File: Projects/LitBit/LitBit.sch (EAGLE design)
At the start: 1 part

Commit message: almost milestoneeeE??
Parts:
- removed U$1: ATMEGA32U4-AU, adafruit:ATMEGA32U4-AU
- added C1, C18, C19: 10uF, SCADA_CUSTOM_LIBRARY:CAP_POL_0603
- added C10, C11, C15: 100nF, SCADA_CUSTOM_LIBRARY:CAP_NONPOL_0603
- added C12, C13, C16, C17, C7, C8: 12p, SCADA_CUSTOM_LIBRARY:CAP_NONPOL_0603
- added C14, C26: 1uF, SCADA_CUSTOM_LIBRARY:CAP_NONPOL_0603
- added C2, C25, C3: 4.7uF, SCADA_CUSTOM_LIBRARY:CAP_NONPOL_0603
- added C20: 1 nF, SCADA_CUSTOM_LIBRARY:CAP_NONPOL_0603
- added C21: 1.2 pF, SCADA_CUSTOM_LIBRARY:CAP_NONPOL_0603
- added C22: 1.5 pF, SCADA_CUSTOM_LIBRARY:CAP_NONPOL_0603
- added C23: 1.8 pF, SCADA_CUSTOM_LIBRARY:CAP_NONPOL_0603
- added C24: 2.2 nF, SCADA_CUSTOM_LIBRARY:CAP_NONPOL_0603
- added C27, C4, C5, C6: 100n, SCADA_CUSTOM_LIBRARY:CAP_NONPOL_0603
- added C28, C29: 22p, SCADA_CUSTOM_LIBRARY:CAP_NONPOL_0603
- added C9: 33nF, SCADA_CUSTOM_LIBRARY:CAP_NONPOL_0603
- added D1: Green, Wurth_Elektronik_Optoelectronics_rev18a:WL-SMCW-150060GS75000
- added FB1, FB2: (no value), SCADA_CUSTOM_LIBRARY:FERRITE
- added ISP1: AVRISP-6, adafruit:AVRISP-6
- added JMP1: 0R-JUMPA, SCADA_CUSTOM_LIBRARY:0R-JUMPA
- added JP1, JP10, JP2, JP3, JP4, JP5, JP6, JP7, JP9: (no value), microbuilder:JUMPER2
- added JP11: BLE_SPI, jumper:JP3Q
- added JP12: Display, adafruit:PINHD-1X6
- added JP8: I2c, pinhead:PINHD-1X2
- added L1: 15 nH, SCADA_CUSTOM_LIBRARY:IND-0603
- added L2: 10 uH, SCADA_CUSTOM_LIBRARY:IND-0805
- added L3: 5.6 nH, SCADA_CUSTOM_LIBRARY:IND-0603
- added L4: 8.2 nH, SCADA_CUSTOM_LIBRARY:IND-0603
- added L5: 3.9 nH, SCADA_CUSTOM_LIBRARY:IND-0603
- added R1: 22k, SCADA_CUSTOM_LIBRARY:RES-0603
- added R2, R7: 0R, SCADA_CUSTOM_LIBRARY:RES-0603
- added R3: 47k, SCADA_CUSTOM_LIBRARY:RES-0603
- added R4: 330, SCADA_CUSTOM_LIBRARY:RES-0603
- added R5, R6, R8: 10k, SCADA_CUSTOM_LIBRARY:RES-0603
- added TP1: TEST_POINT_40MIL_DIA, SCADA_CUSTOM_LIBRARY:TEST_POINT_40MIL_DIA
- added U$28: (no value), microbuilder:ANTENNA_PCBNRF8001_1.6MM
- added U1: 24FC1025, SCADA_CUSTOM_LIBRARY:24FC1025
- added U2: MCP7490N, SCADA_CUSTOM_LIBRARY:MCP7490N
- added U3: ADXL345, SCADA_CUSTOM_LIBRARY:ADXL345
- added U4: ATMEGA32U4-AU, SCADA_CUSTOM_LIBRARY:ATMEGA32U4-AU
- added U5: S-1335J33-M5T1U3, SCADA_CUSTOM_LIBRARY:S-1335J33-M5T1U3
- added U6: nRF8001, microbuilder:NRF8001
- added U7: MCP73831, SCADA_CUSTOM_LIBRARY:MCP73831
- added USB1: ZX62-B-5PA, Seeed-Connector:MICRO-USB-SMD(ZX62-B-5PA)
- added Y1: 16.0000 MHz, SCADA_CUSTOM_LIBRARY:FA-238_CRYSTAL
- added Y2, Y3: 32.7680 kHz, SCADA_CUSTOM_LIBRARY:ABS25_CRYSTAL
- added Y4: 8.0000 MHz, adafruit:CRYSTALHC49UP
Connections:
- new net 3.3V: C19.+, FB1.P$1, ISP1.VCC, JMP1-0R.3, JP2.2, JP3.2, JP5.2, JP9.2, R5.2, R6.2, R7.1, U5.VOUT
- new net ACTIVE: U6A.ACTIVE
- new net AGND: R2.1, U3.GND
- new net AVCC: JP10.2, JP7.2, R7.2
- new net D+: U4.D+, USB1.D+
- new net D-: U4.D-, USB1.D-
- new net MFP: R8.1, U2.MFP
- new net MISO: ISP1.MISO, JP11.5
- new net MISO_3V3: JP11.6, U6A.MISO
- new net MOSI: ISP1.MOSI, JP11.3, U4.PB2(PDI/MOSI)
- new net MOSI_3V3: JP11.4, U6A.MOSI
- new net N$1: C7.2, U2.X1, Y3.2
- new net N$10: L1.1, L2.2
- new net N$11: L2.1, U6A.DCC
- new net N$12: C16.1, U6A.XC1, Y1.2
- new net N$13: JMP1-0R.2, U5.SST
- new net N$14: C18.+, JP1.1, U5.ON/OFF, U5.VIN
- new net N$15: C4.1, JP2.1, R8.2, U2.VCC
- new net N$16: C3.1, JP4.1, U7.VBAT
- new net N$17: C26.1, C5.1, JP3.1, U1.A2, U1.VCC
- new net N$18: C17.1, U6A.XC2, Y1.1
- new net N$19: C23.2, L5.2
- new net N$2: C8.2, U2.X2, Y3.1
- new net N$20: L4.2, L5.1, U6A.ANT2
- new net N$21: L3.1, L4.1, U6A.ANT1
- new net N$22: R1.1, U6A.IREF
- new net N$23: C24.1, L3.2, U6A.VDD_PA
- new net N$24: C21.1, C22.1, C23.1, U$28.P$1
- new net N$25: D1.-, R4.2
- new net N$26: R3.2, U7.PROG
- new net N$27: R4.1, U7.STAT
- new net N$28: C25.1, JP9.1, U4.VCC, U4.VCC1
- new net N$29: C28.2, U4.XTAL2, Y4.1
- new net N$3: C10.1, U6A.DEC1
- new net N$30: C29.2, U4.XTAL1, Y4.2
- new net N$32: FB2.P$2, JP10.1
- new net N$33: C27.1, FB2.P$1, U4.AVCC, U4.AVCC1
- new net N$34: TP1.P$1, U4.AREF
- new net N$4: C9.1, U6A.DEC2
- new net N$5: C12.2, U6A.XL2, Y2.2
- new net N$6: C13.2, U6A.XL1, Y2.1
- new net N$7: C2.1, D1.+, JP6.1, U7.VDD
- new net N$8: C1.+, C15.1, JP5.1, U6A.VDD@1, U6A.VDD@2
- new net N$9: C6.2, JP7.1, U3.VS
- new net RDYN: U6A.RDYN
- new net REQN_3V3: U6A.REQN
- new net RST: ISP1.RST, U4./RESET
- new net RST_NRF: U6A.RESET
- new net SCK: ISP1.SCK, JP11.1, U4.PB1(SCK)
- new net SCK_3V3: JP11.2, U6A.SCK
- new net SCL: JP8.2, R5.1, U1.SCL, U2.SCL, U3.SCL, U4.PD0(INT0/OC0B/SCL)
- new net SDA: JP8.1, R6.1, U1.SDA, U2.SDA, U3.SDA, U4.PD1(INT1/SDA)
- new net SHIELD: USB1.GND, USB1.SHIELD
- new net VDDA: C11.1, C14.1, C20.1, FB1.P$2, L1.2, U6A.AVDD@1, U6A.AVDD@2, U6A.AVDD@3
- new net V_BATT: JP1.2, JP4.2
- new net V_USB: JP6.2, U4.VBUS, USB1.VBUS
- net GND: now also C1.-, C10.2, C11.2, C12.1, C13.1, C14.2, C15.2, C16.2, C17.2, C18.-, C19.-, C2.2, C20.2, C21.2, C22.2, C24.2, C25.2, C26.2, C27.2, C28.1, C29.1, C3.2, C4.2, C5.2, C6.1, C7.1, C8.1, C9.2, ISP1.GND, JMP1-0R.1, R1.2, R2.2, R3.1, U1.A0, U1.A1, U1.VSS, U1.WP, U2.VBAT, U2.VSS, U4.GND, U4.GND1, U4.GND2, U4.GND3, U4.UGND, U5.VSS, U6-SLUG.TP, U6A.VSS@1, U6A.VSS@2, U6A.VSS@3, U6A.VSS@4, U6A.VSS@5, U6A.VSS@6, U7.VSS; no longer U$1.GND, U$1.GND1, U$1.GND2, U$1.GND3
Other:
- note added: "SPI MODE 0"
- note added: "but RDYN and REQN"
- note added: "replace CS"

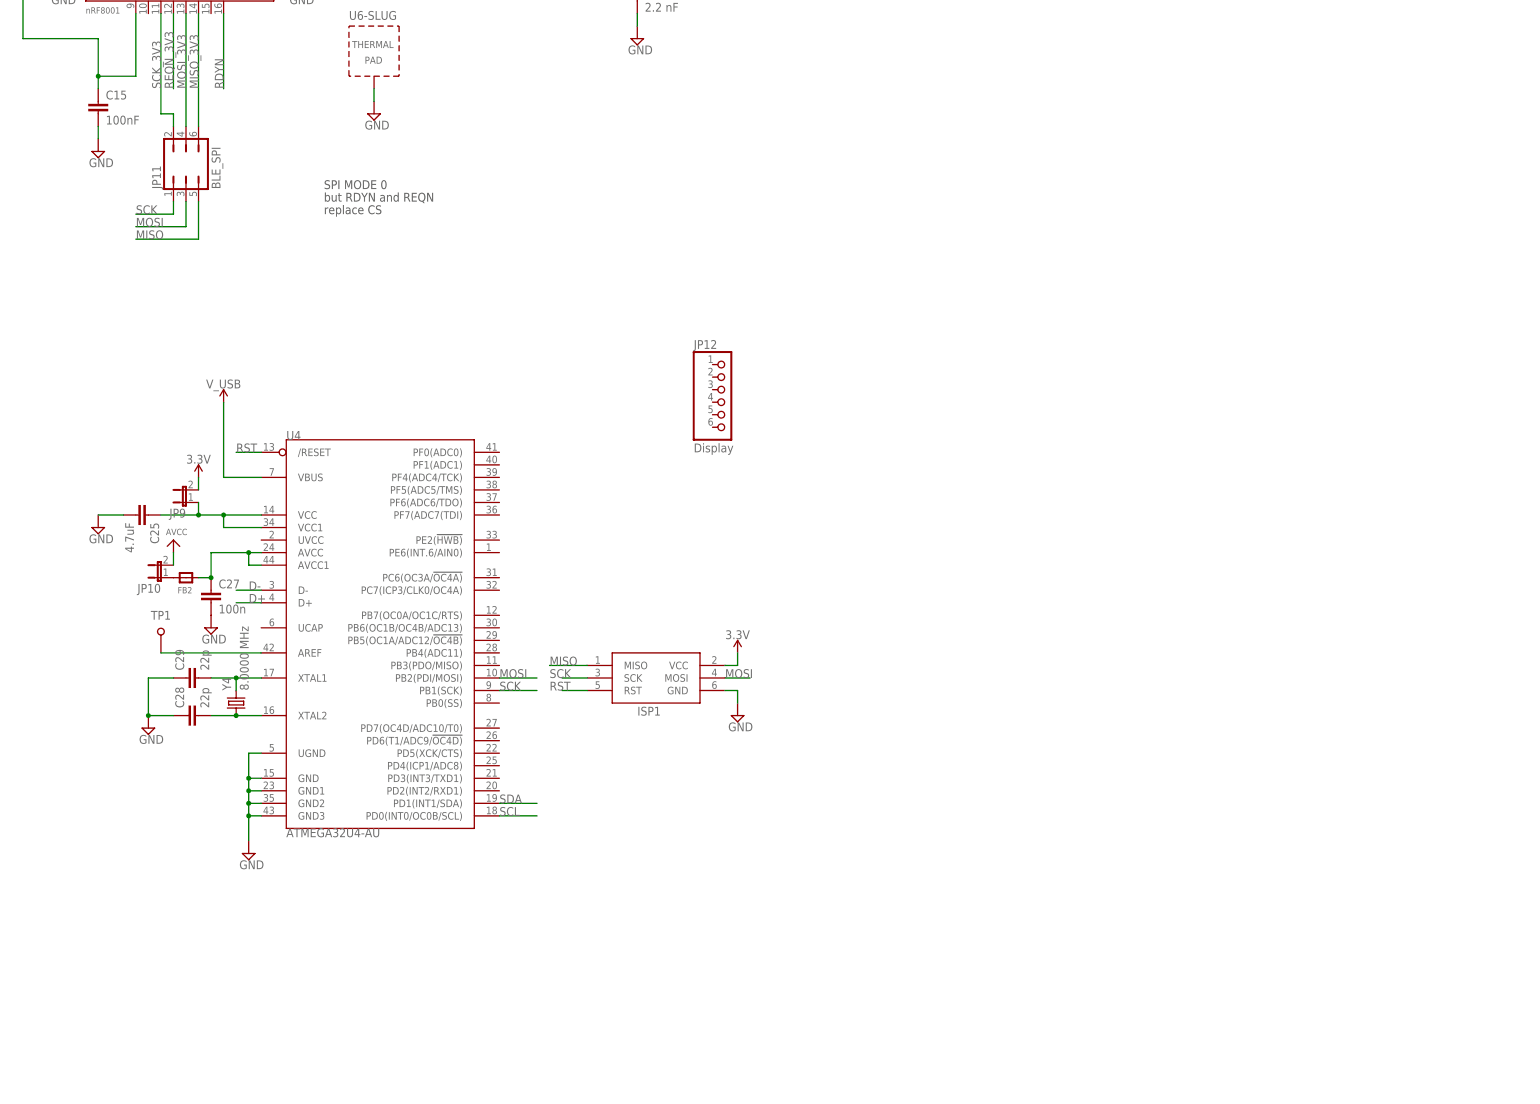
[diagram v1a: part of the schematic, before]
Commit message: Change processor package to VQFN to save space.
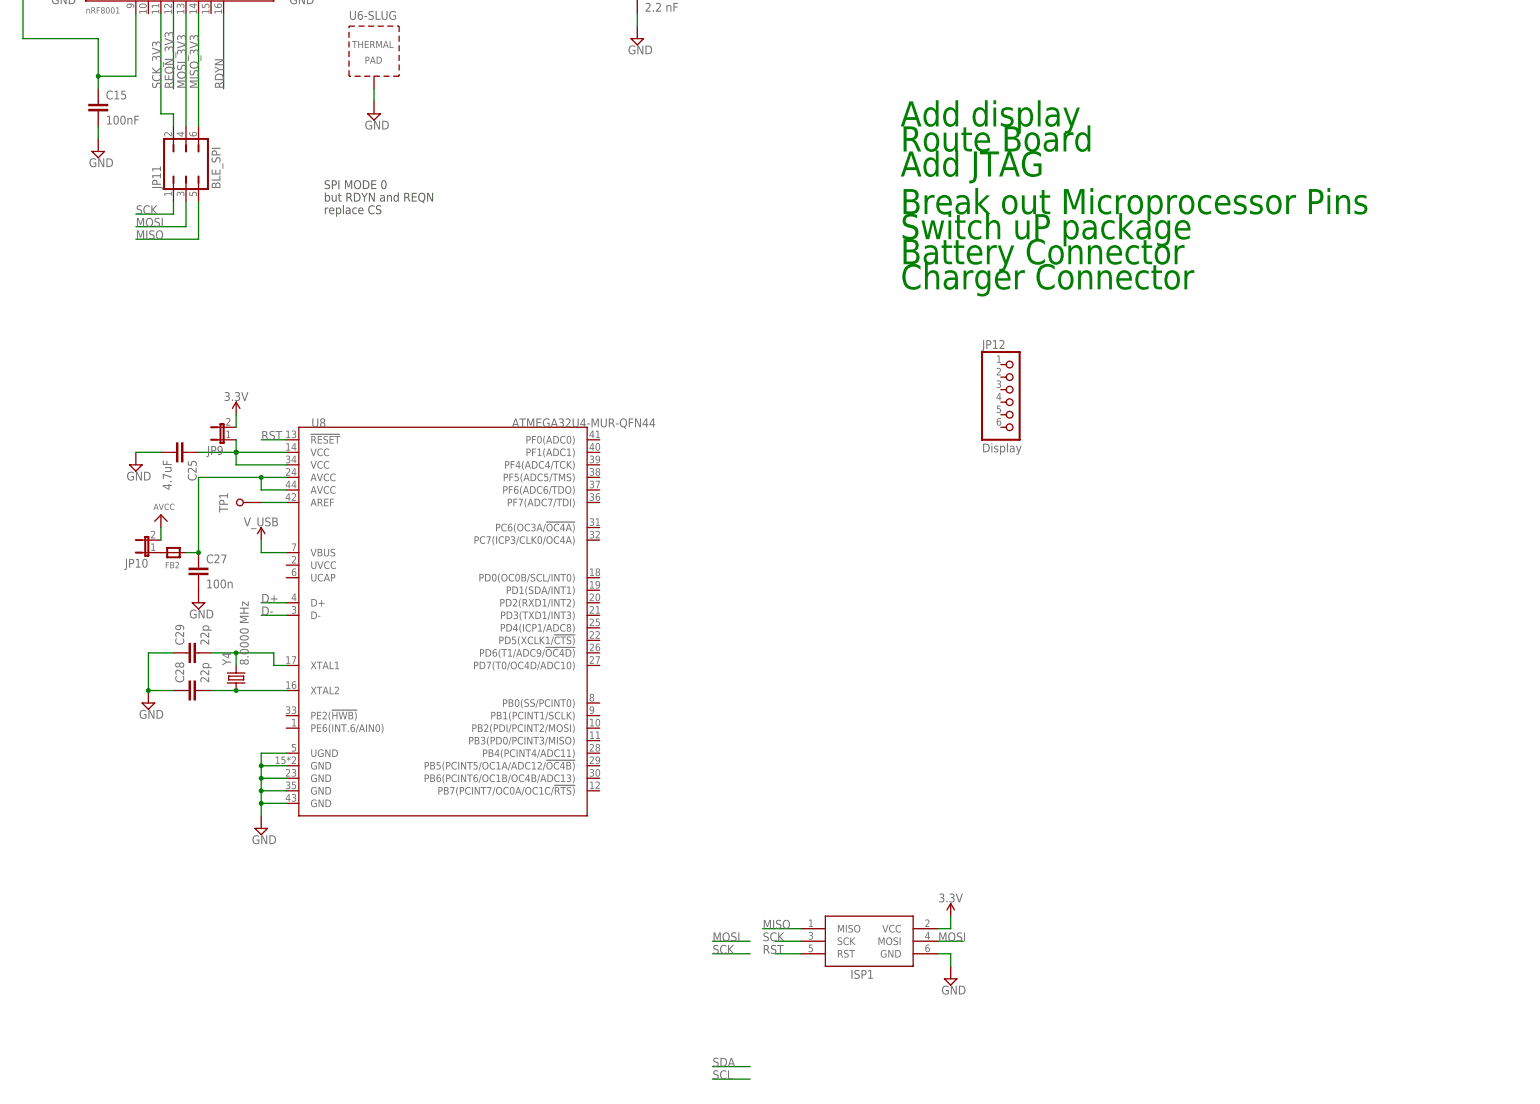
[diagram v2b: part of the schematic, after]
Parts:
- removed U4: ATMEGA32U4-AU, SCADA_CUSTOM_LIBRARY:ATMEGA32U4-AU
- added U8: ATMEGA32U4-MUR-QFN44, Seeed-IC:MCU-ATMEGA32U4-MUR(VQFN44)
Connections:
- net D+: now also U8.D+; no longer U4.D+
- net D-: now also U8.D-; no longer U4.D-
- net GND: now also U8.GND@1, U8.GND@2, U8.GND@3, U8.GND@4, U8.UGND; no longer U4.GND, U4.GND1, U4.GND2, U4.GND3, U4.UGND
- net MOSI: no longer U4.PB2(PDI/MOSI)
- net N$28: now also U8.VCC@1, U8.VCC@2; no longer U4.VCC, U4.VCC1
- net N$29: now also U8.XTAL2; no longer U4.XTAL2
- net N$30: now also U8.XTAL1; no longer U4.XTAL1
- net N$33: now also U8.AVCC@1, U8.AVCC@2; no longer U4.AVCC, U4.AVCC1
- net N$34: no longer U4.AREF
- net RST: now also U8.!RESET; no longer U4./RESET
- net SCK: no longer U4.PB1(SCK)
- net SCL: no longer U4.PD0(INT0/OC0B/SCL)
- net SDA: no longer U4.PD1(INT1/SDA)
- net V_USB: now also U8.VBUS; no longer U4.VBUS
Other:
- note added: "Add JTAG"
- note added: "Add display"
- note added: "Battery Connector"
- note added: "Break out Microprocessor Pins"
- note added: "Charger Connector"
- note added: "Route Board"
- note added: "Switch uP package"
- moved on the sheet: C25, C27, C28, C29, FB2, ISP1, JP10, JP12, JP9, TP1, Y4

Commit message: Start Layout, change uP package, add display, add JTAG, add battery connector.
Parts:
- removed D1: Green, Wurth_Elektronik_Optoelectronics_rev18a:WL-SMCW-150060GS75000
- removed JP10, JP4, JP5, JP6, JP7, JP9: (no value), microbuilder:JUMPER2
- removed JP11: BLE_SPI, jumper:JP3Q
- removed JP12: Display, adafruit:PINHD-1X6
- removed R7: 0R, SCADA_CUSTOM_LIBRARY:RES-0603
- removed TP1: TEST_POINT_40MIL_DIA, SCADA_CUSTOM_LIBRARY:TEST_POINT_40MIL_DIA
- removed Y4: 8.0000 MHz, adafruit:CRYSTALHC49UP
- added C30, C31, C34: 1uF, SCADA_CUSTOM_LIBRARY:CAP_NONPOL_0603
- added C32: 10uF, SCADA_CUSTOM_LIBRARY:CAP_POL_0603
- added C33: 100n, SCADA_CUSTOM_LIBRARY:CAP_NONPOL_0603
- added CHRG: Green, SCADA_CUSTOM_LIBRARY:LED_WL-SMCW-150060GS75000
- added J1: Battery, SparkFun-Connectors:CONN_02-JST-2MM-SMT
- added Q1: CSTCR6M00G53Z, murata-filter:CSTCR6M00G53Z
- added R10, R11, R12, R13, R14, R9: 10k, SCADA_CUSTOM_LIBRARY:RES-0603
- added R15, R16, R17, R18, R19, R20, R21, R22, R23, R24: 0, SCADA_CUSTOM_LIBRARY:RES-0603
- C26: value 1uF -> 4.7 uF
- C28: value 22p -> 100n
- C29: value 22p -> 4.7uF
- JP1: value (none) -> Display; device microbuilder:JUMPER2 -> pinhead:PINHD-1X4
- JP2: device microbuilder:JUMPER2 -> pinhead:PINHD-2X3
- JP3: value (none) -> JTAG; device microbuilder:JUMPER2 -> pinhead:PINHD-2X5
- R5, R6: value 10k -> 2.2k
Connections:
- removed net N$28: C25.1, JP9.1, U8.VCC@1, U8.VCC@2
- removed net N$32: FB2.P$2, JP10.1
- removed net N$33: C27.1, FB2.P$1, U8.AVCC@1, U8.AVCC@2
- removed net N$34: TP1.P$1
- removed net N$9: C6.2, JP7.1, U3.VS
- removed net SHIELD: USB1.GND, USB1.SHIELD
- new net ADXL_INT1: U3.INT1, U8.PD3(TXD1/INT3)
- new net ADXL_INT2: U3.INT2, U8.PD4(ICP1/ADC8)
- new net CHRG_IN: C2.1, CHRG.+, R15.2, U7.VDD
- new net N$36: C32.+, C33.1, C6.2, R21.2, U3.VDD_I/O, U3.VS
- new net TCK: JP3.1, R10.1, U8.PF4(ADC4/TCK)
- new net TDI: JP3.9, R11.1, U8.PF7(ADC7/TDI)
- new net TDO: JP3.3, R12.1, U8.PF6(ADC6/TDO)
- new net TMS: JP3.5, R9.1, U8.PF5(ADC5/TMS)
- new net UP_AVCC: C27.1, C29.2, R23.2, U8.AVCC@1, U8.AVCC@2
- new net UP_D+: R14.1, U8.D+
- new net UP_D-: R13.1, U8.D-
- new net UP_PWR: C25.1, C28.1, C30.2, JP3.4, R10.2, R11.2, R12.2, R22.2, R9.2, U8.UCAP, U8.VCC@1, U8.VCC@2
- new net UVCC: U8.UVCC
- net 3.3V: now also FB2.P$2, R18.1, R19.1, R20.1, R22.1, R24.1, U3./CS; no longer JP2.2, JP3.2, JP5.2, JP9.2, R7.1
- net ACTIVE: now also U8.PB7(PCINT7/OC0A/OC1C/!RTS)
- net AGND: now also C27.2, C29.1, C32.-, C33.2, C34.2, C6.1, R2.2, U8.AREF; no longer R2.1
- net AVCC: now also C34.1, FB2.P$1, R21.1, R23.1; no longer JP10.2, JP7.2, R7.2
- net D+: now also R14.2; no longer U8.D+
- net D-: now also R13.2; no longer U8.D-
- net GND: now also C28.2, C30.1, C31.2, J1.1, JP1.4, JP3.10, JP3.2, Q1.2, R2.1, U3.SDO, USB1.GND, USB1.SHIELD; no longer C27.2, C28.1, C29.1, C6.1, R2.2
- net MISO: now also JP2.2, U8.PB3(PD0/PCINT3/MISO); no longer JP11.5
- net MISO_3V3: now also JP2.1; no longer JP11.6
- net MOSI: now also JP2.4, U8.PB2(PDI/PCINT2/MOSI); no longer JP11.3
- net MOSI_3V3: now also JP2.3; no longer JP11.4
- net N$14: now also R17.2; no longer JP1.1
- net N$15: now also R19.2; no longer JP2.1
- net N$16: now also R16.2; no longer JP4.1
- net N$17: now also R20.2; no longer JP3.1
- net N$25: now also CHRG.-; no longer D1.-
- net N$29: now also Q1.1, U8.XTAL1; no longer C28.2, U8.XTAL2, Y4.1
- net N$30: now also Q1.3, U8.XTAL2; no longer C29.2, U8.XTAL1, Y4.2
- net N$7: now also JP1.3, R24.2; no longer C2.1, D1.+, JP6.1, U7.VDD
- net N$8: now also R18.2; no longer JP5.1
- net RDYN: now also U8.PD2(RXD1/INT2)
- net RST: now also JP3.6
- net RST_NRF: now also U8.PB0(SS/PCINT0)
- net SCK: now also JP2.6, U8.PB1(PCINT1/SCLK); no longer JP11.1
- net SCK_3V3: now also JP2.5; no longer JP11.2
- net SCL: now also JP1.1, U8.PD0(OC0B/SCL/INT0)
- net SDA: now also JP1.2, U8.PD1(SDA/INT1)
- net V_BATT: now also J1.2, R16.1, R17.1; no longer JP1.2, JP4.2
- net V_USB: now also C31.1, R15.1; no longer JP6.2
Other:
- note added: "Investigate RDYN and REQN"
- moved on the sheet: C11, C27, C28, C29, C6, FB1, FB2, R2, U3

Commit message: routing, change RTC package
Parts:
- removed C25, C29: 4.7uF, SCADA_CUSTOM_LIBRARY:CAP_NONPOL_0603
- removed C27, C28: 100n, SCADA_CUSTOM_LIBRARY:CAP_NONPOL_0603
- removed C30: 1uF, SCADA_CUSTOM_LIBRARY:CAP_NONPOL_0603
- removed ISP1: AVRISP-6, adafruit:AVRISP-6
- removed Q1: CSTCR6M00G53Z, murata-filter:CSTCR6M00G53Z
- removed R10, R11, R12, R13, R14, R9: 10k, SCADA_CUSTOM_LIBRARY:RES-0603
- removed R22, R23: 0, SCADA_CUSTOM_LIBRARY:RES-0603
- removed U8: ATMEGA32U4-MUR-QFN44, Seeed-IC:MCU-ATMEGA32U4-MUR(VQFN44)
- added C35, C38: 4.7uF, SCADA_CUSTOM_LIBRARY:CAP_NONPOL_0603
- added C36, C37: 100n, SCADA_CUSTOM_LIBRARY:CAP_NONPOL_0603
- added C39: 1uF, SCADA_CUSTOM_LIBRARY:CAP_NONPOL_0603
- added GND, U$13: MOUNTINGHOLE2.0, microbuilder:MOUNTINGHOLE2.0
- added ISP: AVRISP-6, adafruit:AVRISP-6
- added Q2: CSTCR6M00G53Z, murata-filter:CSTCR6M00G53Z
- added R25, R26, R27, R7: 10k, SCADA_CUSTOM_LIBRARY:RES-0603
- added R28, R29: 0, SCADA_CUSTOM_LIBRARY:RES-0603
- added R30, R31: 22, SCADA_CUSTOM_LIBRARY:RES-0603
- added U4: UP_ATMEGA32U4-AU, SCADA_CUSTOM_LIBRARY:UP_ATMEGA32U4-AU
- U2: value MCP7490N -> RTC_MCP7940N8-MSOP; device SCADA_CUSTOM_LIBRARY:MCP7490N -> SCADA_CUSTOM_LIBRARY:RTC_MCP7940N8-MSOP
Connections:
- removed net N$29: Q1.1, U8.XTAL1
- removed net N$30: Q1.3, U8.XTAL2
- removed net UP_D+: R14.1, U8.D+
- removed net UP_D-: R13.1, U8.D-
- removed net UVCC: U8.UVCC
- new net N$28: R31.1, USB1.D+
- new net N$31: Q2.1, U4.XTAL2
- new net N$32: Q2.3, U4.XTAL1
- new net N$9: R30.1, USB1.D-
- net 3.3V: now also ISP.VCC, R28.1; no longer ISP1.VCC, R22.1, U3./CS
- net ACTIVE: now also U4.PB7(OC0A/OC1C/RTS); no longer U8.PB7(PCINT7/OC0A/OC1C/!RTS)
- net ADXL_INT1: now also U4.PB6(OC1B/OC4B/ADC13); no longer U8.PD3(TXD1/INT3)
- net ADXL_INT2: now also U4.PB5(OC1A/ADC12/!OC4B); no longer U8.PD4(ICP1/ADC8)
- net AGND: now also C37.2, C38.1, U3.SDO, U4.AREF; no longer C27.2, C29.1, U8.AREF
- net AVCC: now also R29.2, U3./CS; no longer R23.1
- net D+: now also R31.2, U4.D+; no longer R14.2, USB1.D+
- net D-: now also R30.2, U4.D-; no longer R13.2, USB1.D-
- net GND: now also C35.2, C36.2, C39.1, ISP.GND, Q2.2, U4.GND, U4.GND1, U4.GND2, U4.GND3, U4.UGND; no longer C25.2, C28.2, C30.1, ISP1.GND, Q1.2, U3.SDO, U8.GND@1, U8.GND@2, U8.GND@3, U8.GND@4, U8.UGND
- net MFP: now also U4.PD3(INT3/TXD1)
- net MISO: now also ISP.MISO, U4.PB3(PDO/MISO); no longer ISP1.MISO, U8.PB3(PD0/PCINT3/MISO)
- net MOSI: now also ISP.MOSI, U4.PB2(PDI/MOSI); no longer ISP1.MOSI, U8.PB2(PDI/PCINT2/MOSI)
- net RDYN: now also U4.PD2(INT2/RXD1); no longer U8.PD2(RXD1/INT2)
- net RST: now also ISP.RST, U4./RESET; no longer ISP1.RST, U8.!RESET
- net RST_NRF: now also U4.PB0(SS); no longer U8.PB0(SS/PCINT0)
- net SCK: now also ISP.SCK, U4.PB1(SCK); no longer ISP1.SCK, U8.PB1(PCINT1/SCLK)
- net SCL: now also U4.PD0(INT0/OC0B/SCL); no longer U8.PD0(OC0B/SCL/INT0)
- net SDA: now also U4.PD1(INT1/SDA); no longer U8.PD1(SDA/INT1)
- net TCK: now also R25.1, U4.PF4(ADC4/TCK); no longer R10.1, U8.PF4(ADC4/TCK)
- net TDI: now also R26.1, U4.PF7(ADC7(TDI); no longer R11.1, U8.PF7(ADC7/TDI)
- net TDO: now also R27.1, U4.PF6(ADC6/TDO); no longer R12.1, U8.PF6(ADC6/TDO)
- net TMS: now also R7.1, U4.PF5(ADC5/TMS); no longer R9.1, U8.PF5(ADC5/TMS)
- net UP_AVCC: now also C37.1, C38.2, R29.1, U4.AVCC, U4.AVCC1; no longer C27.1, C29.2, R23.2, U8.AVCC@1, U8.AVCC@2
- net UP_PWR: now also C35.1, C36.1, C39.2, R25.2, R26.2, R27.2, R28.2, R7.2, U4.UCAP, U4.VCC, U4.VCC1; no longer C25.1, C28.1, C30.2, R10.2, R11.2, R12.2, R22.2, R9.2, U8.UCAP, U8.VCC@1, U8.VCC@2
- net V_USB: now also U4.VBUS; no longer U8.VBUS
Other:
- moved on the sheet: C21, C22, C23, C24, C26, C4, C5, C7, C8, JP1, JP3, JP8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

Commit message: nearly complete layout
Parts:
- removed R28: 0, SCADA_CUSTOM_LIBRARY:RES-0603
- added U$8: MOUNTINGHOLE2.0, microbuilder:MOUNTINGHOLE2.0
- Y2, Y3: device SCADA_CUSTOM_LIBRARY:ABS25_CRYSTAL -> SCADA_CUSTOM_LIBRARY:CRYSTAL_ABS07
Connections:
- removed net N$15: C4.1, R19.2, R8.2, U2.VCC
- removed net UP_PWR: C35.1, C36.1, C39.2, JP3.4, R25.2, R26.2, R27.2, R28.2, R7.2, U4.UCAP, U4.VCC, U4.VCC1
- new net N$29: C4.1, R19.2, U2.VCC
- net 3.3V: now also C35.1, C36.1, C39.2, JP3.4, R25.2, R26.2, R27.2, R7.2, R8.2, U4.UCAP, U4.VCC, U4.VCC1; no longer R28.1
- net N$5: now also Y2.1; no longer Y2.2
- net N$6: now also Y2.2; no longer Y2.1
- net REQN_3V3: now also U4.PE6(INT.6/AIN0)
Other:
- moved on the sheet: Y2
